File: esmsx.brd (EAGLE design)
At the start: 92.7 x 63.5 mm, 28 parts, among them IC1 XC9536_44VQ, IC2 317EMP, U1 PIC32MX130F064D-I/PT

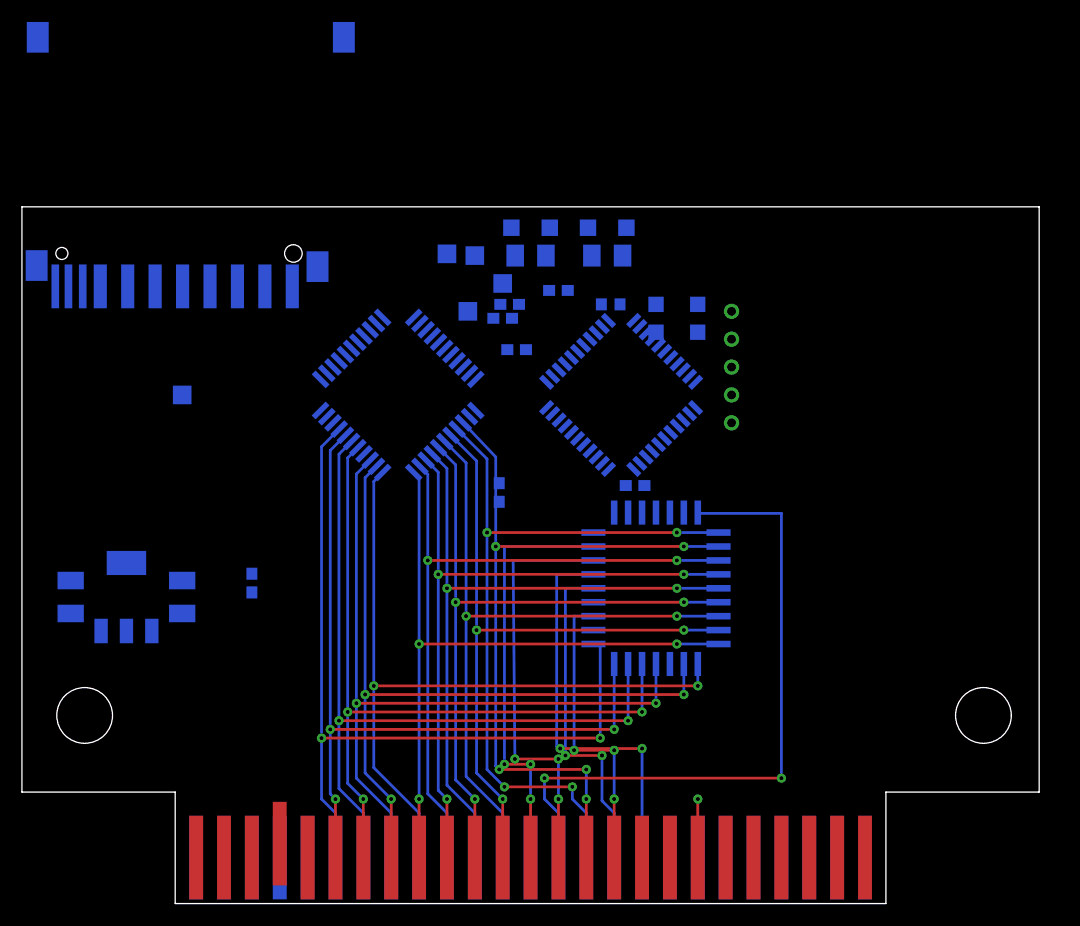
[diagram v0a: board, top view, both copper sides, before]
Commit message: more routing, adding a14,15
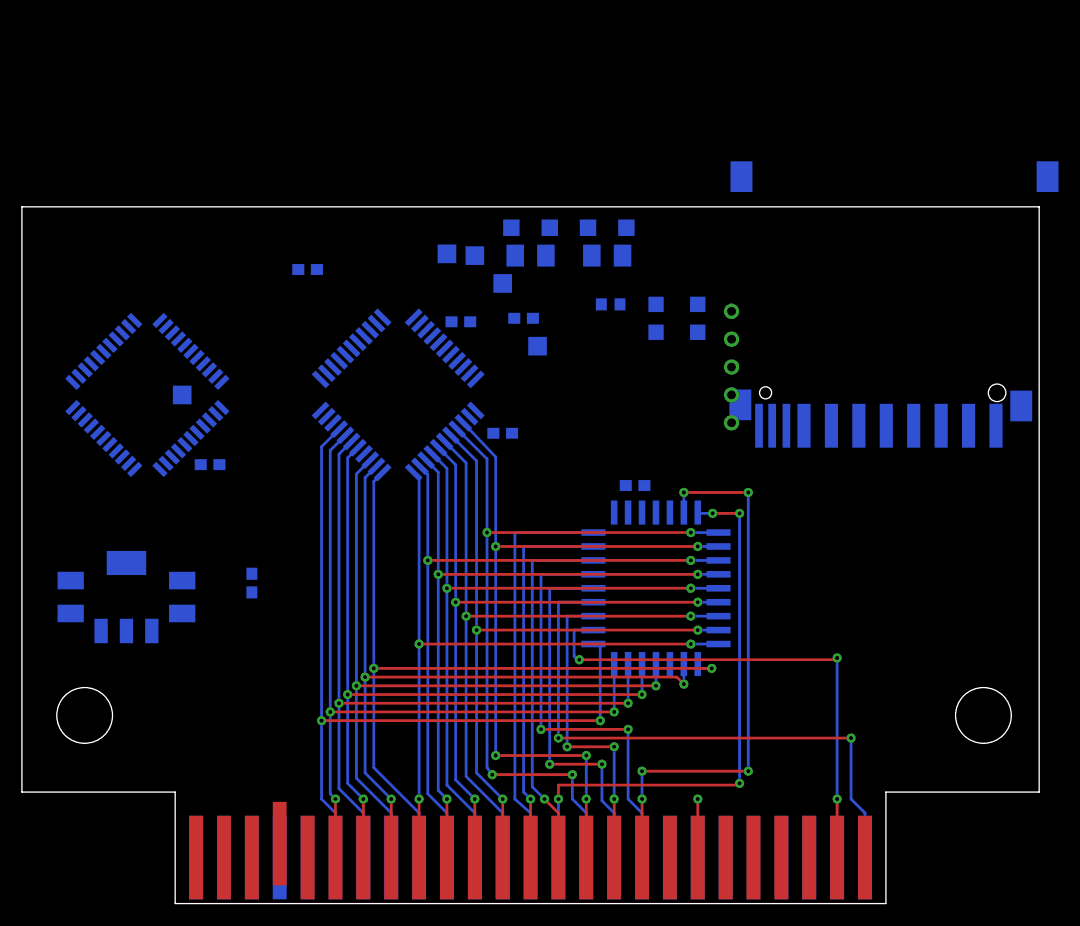
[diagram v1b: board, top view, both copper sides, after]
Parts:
- moved U$4 65.4 mm to (80.6, 45.7)
- moved U1 43.2 mm to (12.7, 47.6), turned to 45 degrees
- moved C9 31.0 mm to (18.4, 41.3), turned to 180 degrees
- moved C10 22.9 mm to (27.3, 59.1)
- moved TP4 7.10 mm to (48.3, 52.1)
- moved C4 5.68 mm to (41.3, 54.3)
- moved C7 5.41 mm to (45.1, 44.1), turned to 180 degrees
- moved C6 1.91 mm to (47.0, 54.6)
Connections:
- removed net !RD: 64KX8.24
- removed net !ROMCS: 64KX8.22
- new net !ROMCE: 64KX8.22, JP1./SLTSL
- new net !ROMOE: 64KX8.24, JP1./CS1
- net A14: now also JP1.A14
- net A15: now also JP1.A15
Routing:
- net !ROMOE: track 0.00 -> 53.7 mm, vias 0 -> 2
- net A15: track 0.00 -> 50.7 mm, vias 0 -> 5
- net !ROMCE: track 0.00 -> 46.7 mm, vias 0 -> 3
- net A14: track 0.00 -> 37.4 mm
- net A12: track 61.1 -> 51.7 mm, vias 2 -> 4
- net A8: track 38.4 -> 33.6 mm, vias 3 -> 1
- net A13: track 38.8 -> 35.0 mm, vias 3 -> 1
- net A11: track 30.9 -> 33.7 mm
- net A9: track 36.8 -> 39.1 mm
- net HOSTD7: track 74.8 -> 73.3 mm
- net HOSTD6: track 71.1 -> 69.5 mm
- net HOSTD5: track 70.8 -> 69.3 mm
- net HOSTD4: track 69.5 -> 67.9 mm
- net HOSTD3: track 68.9 -> 67.4 mm
- net A10: track 27.4 -> 28.7 mm
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
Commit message: more routing
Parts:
- removed TP4, TP5: TPTP17SQ, testpad:TP17SQ
- C10, C3, C4, C5, C6, C7, C9: device rcl:C0603 -> rcl:C0805
- moved U$1 63.2 mm to (3.71, 39.4)
- moved R4 50.8 mm to (5.71, 43.2), turned to 270 degrees
- moved R3 50.8 mm to (3.81, 59.1), turned to 90 degrees
- moved C5 49.8 mm to (9.53, 54.0), turned to 45 degrees
- moved LED-RED 49.5 mm to (5.08, 62.9), flipped to the top
- moved R1 41.3 mm to (6.35, 59.1), turned to 90 degrees
- moved C6 39.8 mm to (9.53, 41.1), turned to 315 degrees
- moved LED-WHITE 36.2 mm to (11.4, 62.9), flipped to the top
- moved TP3 30.3 mm to (21.4, 38.6), turned to 45 degrees
- moved TP1 23.3 mm to (24.1, 47.6), turned to 45 degrees
- moved C3 22.9 mm to (22.7, 53.3), turned to 135 degrees
- moved TP2 9.79 mm to (25.6, 49.1), turned to 45 degrees
- moved C10 6.25 mm to (27.7, 52.8), turned to 0 degrees
- moved C9 3.18 mm to (21.6, 41.3), turned to 225 degrees
- moved U1 3.18 mm to (15.9, 47.6)
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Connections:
- removed net N$2: IC1.28, TP4.TP
- removed net N$3: IC1.29, TP5.TP
- removed net VCC: 64KX8.31, 64KX8.32
- net !IORQ: now also JP1./IORQ
- net 5V0: now also 64KX8.31, 64KX8.32
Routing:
- net !IORQ: track 0.00 -> 88.1 mm, vias 0 -> 6
- net !NWR: track 0.00 -> 81.8 mm, vias 0 -> 6
- net !RESET: track 0.00 -> 80.9 mm, vias 0 -> 4
- net !NRD: track 5.33 -> 80.2 mm, vias 1 -> 7
- net TDO: track 0.00 -> 33.9 mm, vias 0 -> 2
- net CLIENTD2: track 0.00 -> 30.8 mm, vias 0 -> 2
- net TDI: track 0.00 -> 25.2 mm, vias 0 -> 2
- net TMS: track 0.00 -> 22.8 mm, vias 0 -> 2
- net MISO: track 0.00 -> 22.5 mm, vias 0 -> 1
- net TCK: track 0.00 -> 22.0 mm, vias 0 -> 2
- net MOSI: track 0.00 -> 21.2 mm, vias 0 -> 1
- net CLIENTD3: track 0.00 -> 17.8 mm
- net !CD: track 0.00 -> 17.0 mm, vias 0 -> 1
- net CLIENTD4: track 0.00 -> 16.7 mm
- net !WP: track 0.00 -> 16.3 mm, vias 0 -> 1
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- added copper zone on layer 16, net GND

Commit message: done but for the checking
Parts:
- removed TP1, TP3: TPTP17SQ, testpad:TP17SQ
- removed U$1: PICKIT2-ICSP-5, pickit2:PICKIT2-ICSP-5
- added JP2, JP3: (no value), pinhead-round:1X03
- added U$2: MICROSD_PP, DE1594-v2:MICROSD_PP
- added U$3: 6PIN, SparkFun:1X04-1.27MM
- R1, R3: device resistor:M1206 -> resistor:R0805W
- R4: device rcl:R0603 -> rcl:R0805W
- U$4: value SDMMC06132 -> 5PIN; device adafruit:06132 -> smb-microheaders:1X05-1.27MM
- moved U$4 65.3 mm to (15.9, 37.5), flipped to the top, turned to 0 degrees
- moved D2 58.5 mm to (6.35, 34.9), turned to 90 degrees
- moved D1 55.2 mm to (8.89, 34.9), turned to 90 degrees
- moved TP2 6.05 mm to (24.1, 43.2), turned to 0 degrees
- moved IC2 5.75 mm to (16.5, 28.6)
- moved C1 5.75 mm to (11.4, 28.6)
- moved C2 5.75 mm to (21.6, 28.6)
- moved R4 2.01 mm to (7.62, 42.5), turned to 315 degrees
- moved C10 0.85 mm to (27.9, 53.7), turned to 45 degrees
- moved R3 0.64 mm to (3.17, 59.1)
- moved R1 0.63 mm to (5.71, 59.1)
- moved C7 0.35 mm to (44.8, 43.3)
- moved C6 0.32 mm to (9.21, 41.1)
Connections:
- removed net !WP: U$4.WP, U1.4
- new net N$2: JP1.SW1, JP1.SW2
- new net N$3: 64KX8.31
- new net N$4: U1.21
- new net N$5: U1.24
- net !CD: now also U$2.9; no longer U$4.CD
- net !MCLR': now also U$4.5; no longer U$1.P1
- net !SS: now also U$2.2; no longer U$4.1
- net 3V3: now also U$2.4, U$3.1; no longer U$1.P2
- net 5V0: no longer 64KX8.31
- net GND: now also JP2.1, U$2.6, U$2.GND@1, U$2.GND@2, U$2.GND@3, U$2.GND@4, U$3.2; no longer U$1.P3, U$4.6, U$4.GP, U$4.GP3, U1.41
- net MISO: now also U$2.7; no longer U$4.7
- net MOSI: now also U$2.3; no longer U$4.2
- net PGC: now also U$4.1; no longer U$1.P5
- net PGD: now also U$4.2; no longer U$1.P4
- net RX-S: now also JP3.2; no longer TP3.TP
- net SCK: now also U$2.5; no longer U$4.5
- net TCK: now also U$3.4
- net TDI: now also U$3.5
- net TDO: now also U$3.3
- net TMS: now also U$3.6
- net TX-S: now also JP3.1; no longer TP1.TP
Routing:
- net 3V3: track 15.2 -> 183.2 mm, vias 0 -> 10
- net 5V0: track 0.00 -> 91.6 mm, vias 0 -> 2
- net SCK: track 0.00 -> 81.7 mm, vias 0 -> 2
- net !SS: track 0.00 -> 77.4 mm, vias 0 -> 2
- net TX-S: track 1.94 -> 76.3 mm, vias 0 -> 2
- net RX-S: track 6.44 -> 72.0 mm, vias 0 -> 1
- net MOSI: track 21.2 -> 74.8 mm, vias 1 -> 2
- net !RESET: track 80.9 -> 132.1 mm, vias 4 -> 6
- net MISO: track 22.5 -> 71.7 mm, vias 1 -> 2
- net !CD: track 17.0 -> 65.5 mm, vias 1 -> 2
- net CLIENTD1: track 0.00 -> 37.1 mm, vias 0 -> 2
- net CLIENTD0: track 0.00 -> 32.9 mm, vias 0 -> 2
- net !MCLR: track 0.00 -> 17.0 mm
- net !MCLR': track 0.00 -> 16.5 mm, vias 0 -> 2
- net !WP: track 16.3 -> 0.00 mm, vias 1 -> 0
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- added copper zone on layer 1, net GND
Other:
- board text added: "tx"
- board text removed: "TX"

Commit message: with added logo
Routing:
- net N$42: track 2.86 -> 0.00 mm
- net N$41: track 2.86 -> 0.00 mm
- net N$6: track 2.54 -> 0.00 mm
- net N$20: track 2.54 -> 0.00 mm
- net N$12: track 2.54 -> 0.00 mm
- net N$46: track 2.22 -> 0.00 mm
- net N$45: track 2.22 -> 0.00 mm
- net N$40: track 1.90 -> 0.00 mm
- net N$33: track 1.90 -> 0.00 mm
- net N$31: track 1.90 -> 0.00 mm
- net N$44: track 1.59 -> 0.00 mm
- net N$43: track 1.59 -> 0.00 mm
- net N$7: track 1.27 -> 0.00 mm
- net N$36: track 1.27 -> 0.00 mm
- net N$13: track 1.27 -> 0.00 mm
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
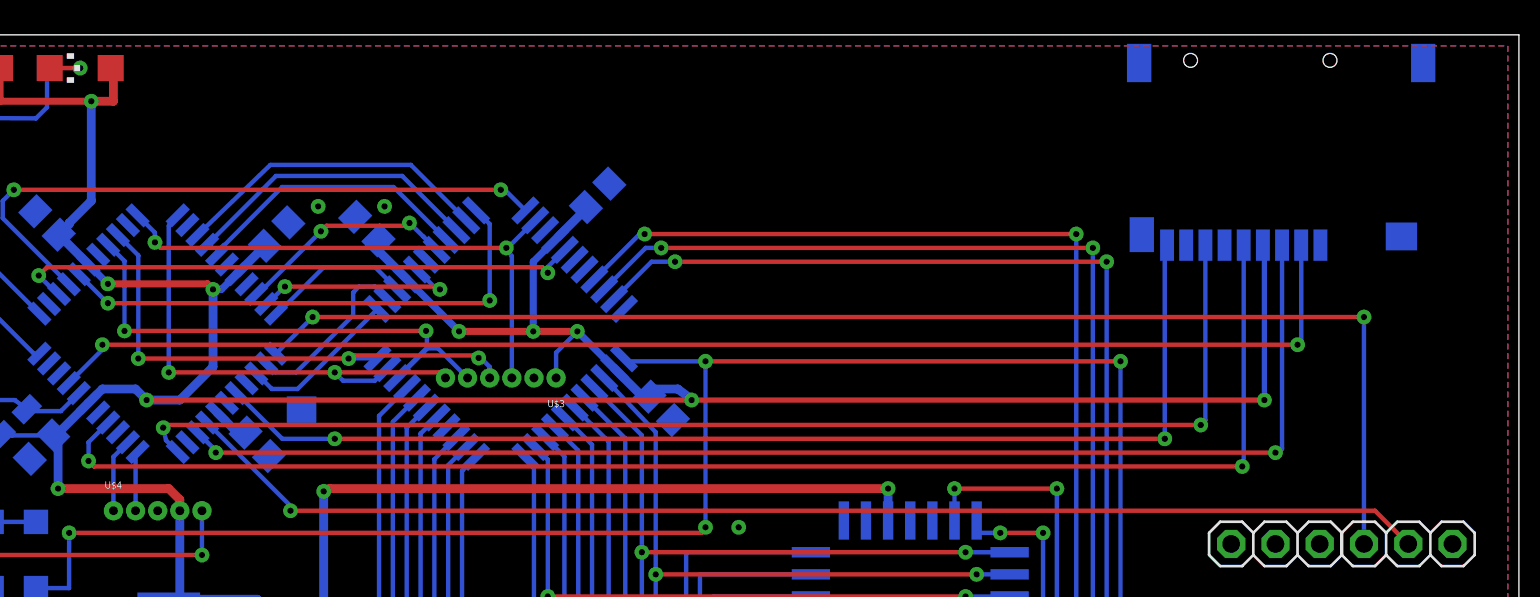
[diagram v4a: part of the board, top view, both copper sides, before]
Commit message: see-through logo done
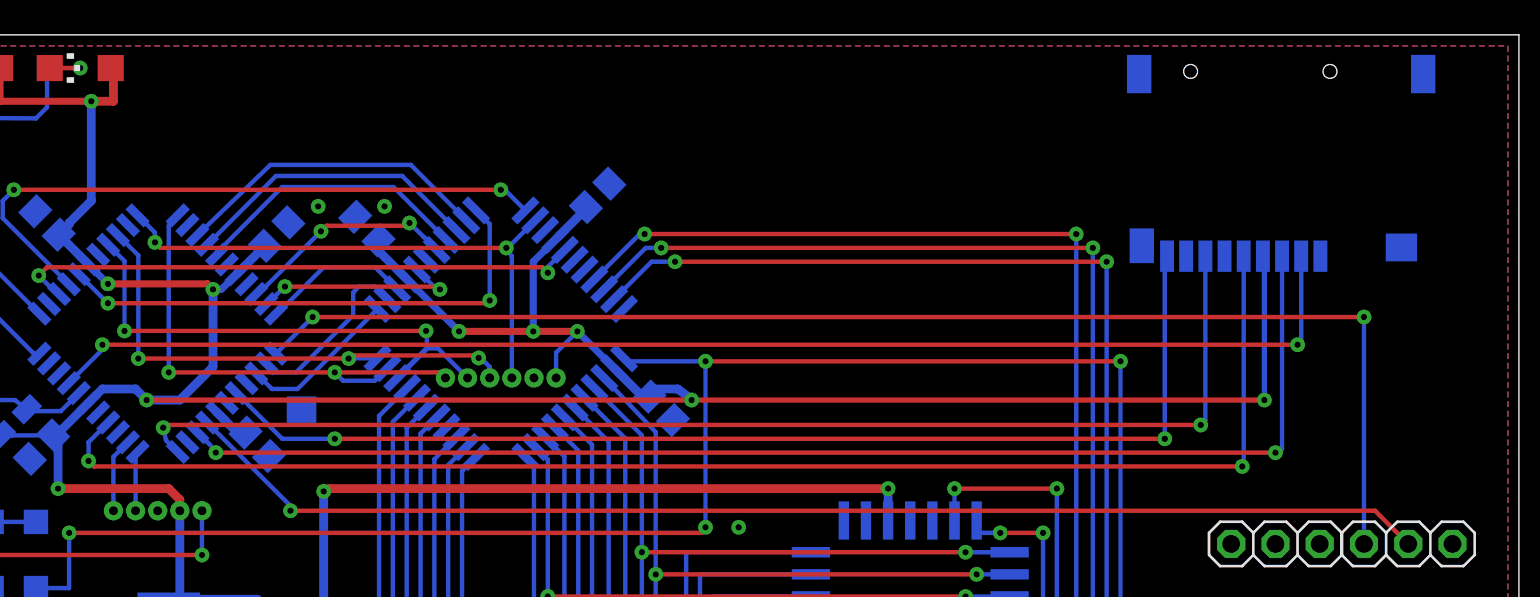
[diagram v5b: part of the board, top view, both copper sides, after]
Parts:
- moved U$2 0.63 mm to (78.7, 52.1)
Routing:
- net SCK: track 81.7 -> 81.1 mm
- net MOSI: track 74.8 -> 74.2 mm
- net MISO: track 71.7 -> 71.1 mm
- net !SS: track 77.4 -> 76.7 mm

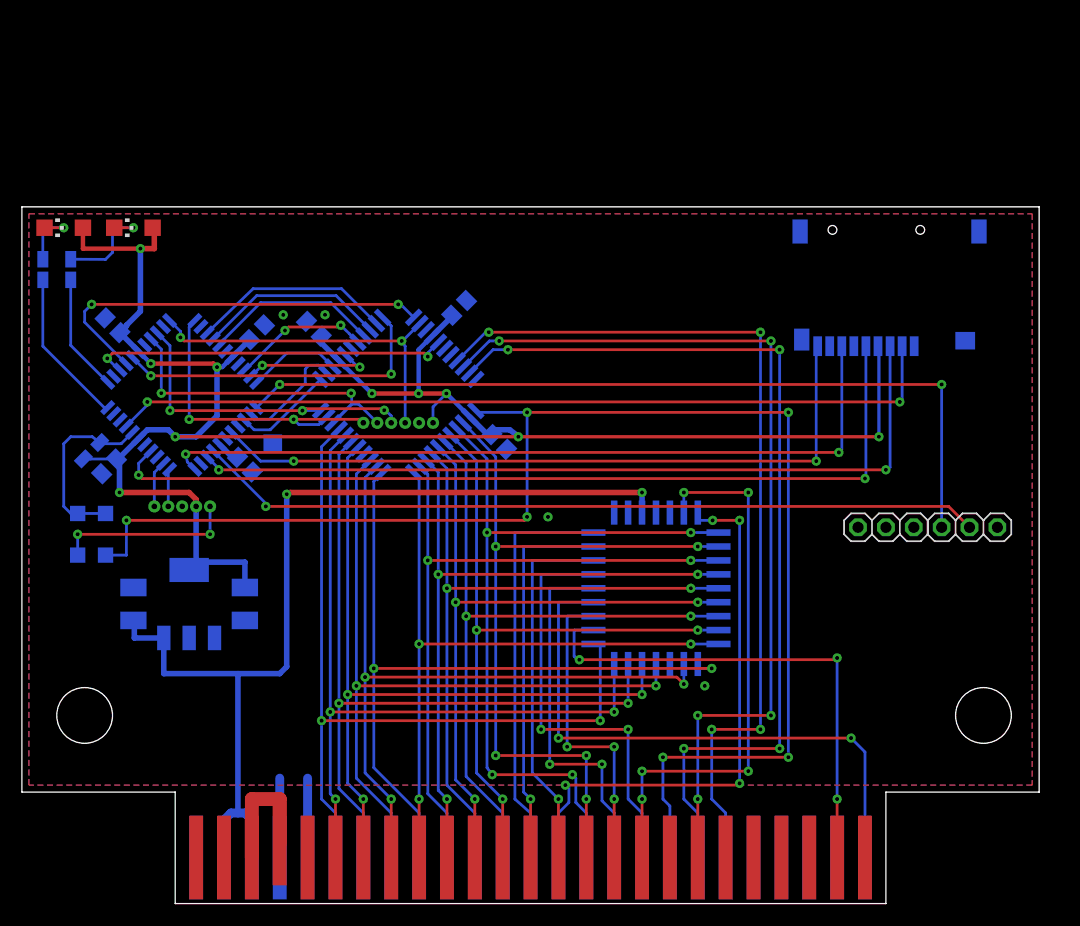
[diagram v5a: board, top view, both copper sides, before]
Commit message: broken out pads and current sources for leds
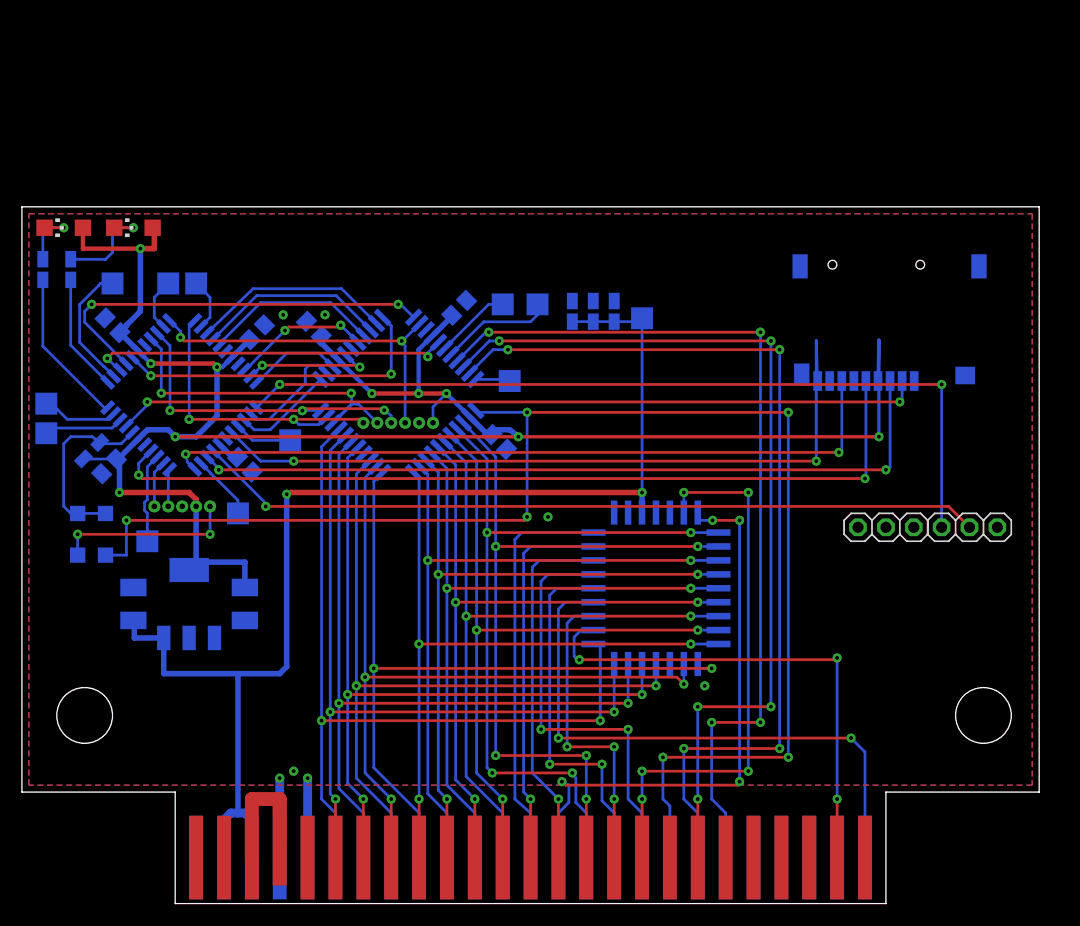
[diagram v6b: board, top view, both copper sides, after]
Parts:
- added R2, R5, R6: (no value), resistor:R0805W
- added TP1, TP10, TP11, TP12, TP3, TP4, TP5, TP6, TP7, TP8, TP9: TPSQTP20SQ, testpad:TP20SQ
- TP2: value TPTP17SQ -> TPSQTP20SQ; device testpad:TP17SQ -> testpad:TP20SQ
- moved TP2 24.5 mm to (45.1, 55.9)
- moved U$2 3.17 mm to (78.7, 48.9)
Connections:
- removed net !M1: IC1.33
- new net N$10: TP6.TP, U1.35
- new net N$12: TP9.TP, U1.20
- new net N$13: TP10.TP, U1.14
- new net N$14: TP11.TP, U1.10
- new net N$15: TP12.TP, U1.4
- new net N$6: IC1.29, TP1.TP
- new net N$7: IC1.28, TP2.TP
- new net N$8: IC1.33, TP3.TP
- new net N$9: TP5.TP, U1.32
- net 5V0: now also R2.1, R5.1, R6.1, TP7.TP
- net GND: no longer TP2.TP
- net N$4: now also TP8.TP
- net N$5: now also TP4.TP
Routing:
- net 5V0: track 91.6 -> 114.0 mm
- net N$5: track 0.00 -> 11.7 mm
- net N$6: track 0.00 -> 10.3 mm
- net N$13: track 0.00 -> 8.26 mm
- net N$12: track 0.00 -> 7.41 mm
- net N$4: track 0.00 -> 6.96 mm
- net N$7: track 0.00 -> 6.94 mm
- net N$14: track 0.00 -> 5.98 mm
- net N$15: track 0.00 -> 5.28 mm
- net N$9: track 0.00 -> 4.80 mm
- net N$10: track 0.00 -> 4.80 mm
- net MOSI: track 74.2 -> 71.0 mm
- net !SS: track 76.7 -> 73.6 mm
- net MISO: track 71.1 -> 67.9 mm
- net SCK: track 81.1 -> 77.9 mm
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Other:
- board text added: "Prototype"
- board text removed: "tx"

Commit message: ordered 29 06 protoype 1
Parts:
- removed TP4: TPSQTP20SQ, testpad:TP20SQ
- added JMP1: 0R-JUMPA, jump-0r-smd:A0R-JMP
- added LED3: (no value), led:CHIPLED_1206
- added R7: (no value), resistor:R0805W
- moved TP7 6.98 mm to (57.8, 47.6)
- moved R2 6.26 mm to (60.6, 52.1), turned to 120 degrees
- moved R6 5.12 mm to (57.8, 52.7)
- moved R5 4.76 mm to (55.0, 52.1), turned to 60 degrees
- moved C1 3.81 mm to (11.4, 24.8)
- moved C2 3.81 mm to (21.6, 24.8)
- moved IC2 3.81 mm to (16.5, 24.8)
- moved JP2 2.54 mm to (77.5, 35.6)
- moved JP3 2.54 mm to (85.1, 35.6)
- renumbered LED-RED to LED1, LED-WHITE to LED2
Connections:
- removed net N$3: 64KX8.31
- removed net N$5: TP4.TP, U1.24
- new net LED-BLUE: R7.1, U1.24
- new net N$11: LED3.C, R7.2
- net !NWR: now also JMP1.3
- net 3V3: now also LED3.A
- net 5V0: now also 64KX8.31, JMP1.1, JMP1.2
- net RX-S: now also JP3.1; no longer JP3.2
- net TX-S: now also JP3.2; no longer JP3.1
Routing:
- net N$11: track 0.00 -> 13.8 mm, vias 0 -> 3
- net !NWR: track 84.7 -> 96.9 mm, vias 4 -> 5
- net N$5: track 11.7 -> 0.00 mm
- net LED-BLUE: track 0.00 -> 10.8 mm
- net !CD: track 69.0 -> 61.7 mm
- net RX-S: track 72.0 -> 67.5 mm
- net 5V0: track 114.0 -> 117.7 mm
- net 3V3: track 186.8 -> 189.9 mm
- net !RESET: track 132.1 -> 131.1 mm
- net !ROMOE: track 53.3 -> 54.0 mm
- net CLIENTD0: track 32.9 -> 33.4 mm
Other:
- board text added: "SMB 2018"

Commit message: name parts in schematic
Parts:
- renumbered IC1 to XC9572XL, U1 to PIC32MX150F128D
